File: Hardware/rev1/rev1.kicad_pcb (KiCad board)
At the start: 4 copper layers, 80 x 22 mm, 45 parts, among them J1 Conn_ARM_JTAG_SWD_10, J2 USB_C_Receptacle_USB2.0_14P, J3 Screw_Terminal_01x02, J4 Conn_01x18_Socket, J5 Conn_01x18_Socket, Q1 AO3400A, SW1 SW_Push, U1 W25Q128JVS, U2 HT75xx-1-SOT89, U3 MS5607-02BA, U4 STM32F103C8Tx, Y1 16MHz

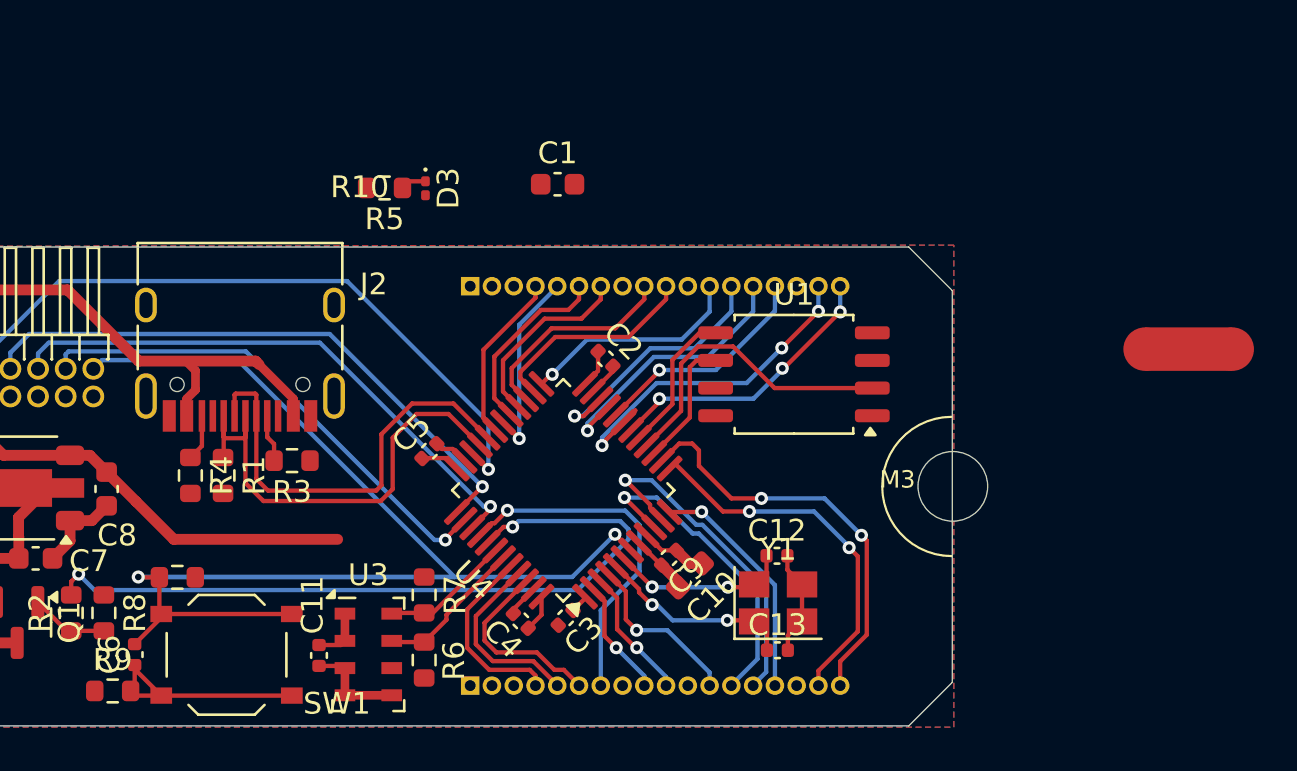
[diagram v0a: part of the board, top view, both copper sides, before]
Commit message: Defenistration Comit
Changed the crystal to be correct, still need to fix the other fixes
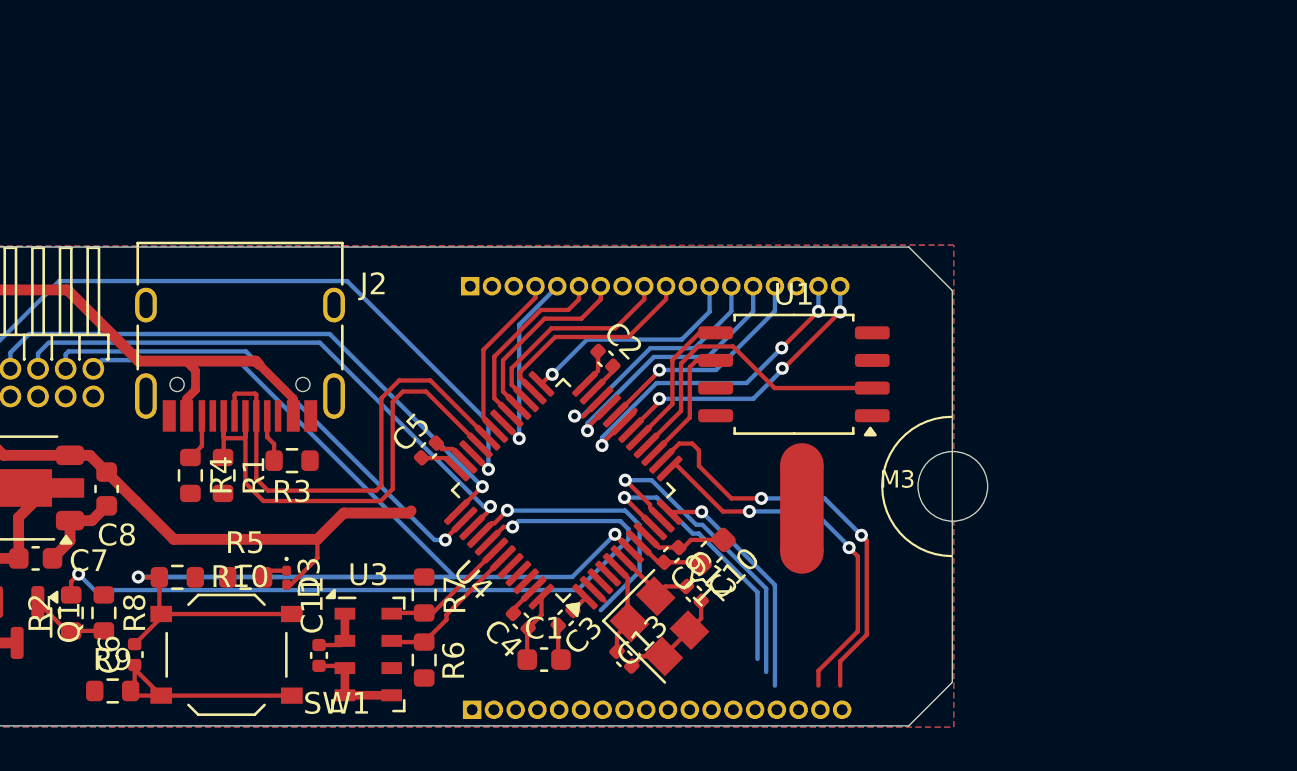
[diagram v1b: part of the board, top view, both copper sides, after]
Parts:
- moved C1 21.8 mm to (174.4, 137.2)
- moved NT1 19.2 mm to (186.2, 130.2), turned to -90 degrees
- moved R5 19.0 mm to (160.7, 133.4)
- moved D3 19.0 mm to (162.6, 133.4)
- moved C13 7.04 mm to (178.1, 137.1), turned to -45 degrees
- moved Y1 5.55 mm to (179.7, 135.6), turned to -45 degrees
- moved C12 4.20 mm to (181.3, 134.1), turned to -45 degrees
- moved C10 1.47 mm to (182.1, 132.2)
- moved J5 1.11 mm to (171.1, 139.5)
- moved C9 0.17 mm to (180.2, 132.3)
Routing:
- net /Microcontroller/PB9: track 8.73 -> 0.00 mm
- net /Microcontroller/BOOTO: track 8.72 -> 0.00 mm
- net /Microcontroller/PB8: track 8.60 -> 0.00 mm
- net +3.3V: track 28.7 -> 36.9 mm
- net /Microcontroller/PC15: track 7.91 -> 0.00 mm, vias 1 -> 0
- net /Microcontroller/PC14: track 6.08 -> 0.00 mm, vias 1 -> 0
- net /Microcontroller/HSE_IN: track 9.53 -> 4.43 mm, vias 2 -> 0
- net /Microcontroller/PC13: track 5.42 -> 0.77 mm, vias 1 -> 0
- net /Microcontroller/HSE_OUT: track 8.52 -> 4.24 mm, vias 2 -> 0
- net /Microcontroller/PB4: track 16.2 -> 12.7 mm
- net GND: track 21.1 -> 23.1 mm
- net /Microcontroller/USB.D-: track 20.4 -> 22.3 mm
- net /Microcontroller/USB.D+: track 22.8 -> 24.6 mm
- net /Microcontroller/PA0: track 14.6 -> 12.9 mm
- net /Microcontroller/PA1: track 15.8 -> 14.9 mm
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
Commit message: No vallium for the whole week :(
Net tie footprint, moved breakouts, crystal we think is close enough, tried to look for debug interface but didn't find it. no vallies :(
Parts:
- removed H3: MountingHole, MountingHole:MountingHole_3.2mm_M3
- NT1: footprint NetTie:NetTie-2_SMD_Pad2.0mm -> NetTie:NetTie-2_SMD_Pad0.5mm
- moved J4 82.2 mm to (120.0, 55.5)
- moved J5 81.3 mm to (120.0, 76.2)
- moved BT1 80.8 mm to (77.8, 65.8)
- moved BZ1 80.8 mm to (94.7, 70.7)
- moved C1 80.8 mm to (124.2, 73.8)
- moved C10 80.8 mm to (131.9, 68.8)
- moved C11 80.8 mm to (113.9, 73.6)
- moved C13 80.8 mm to (127.9, 73.7)
- moved C3 80.8 mm to (125.2, 71.9)
- moved C6 80.8 mm to (105.4, 73.6)
- moved C9 80.8 mm to (130.1, 69.0)
- moved J2 80.8 mm to (110.2, 58.5)
- moved J3 80.8 mm to (91.8, 61.6)
- moved R1 80.8 mm to (109.5, 65.3)
- moved R4 80.8 mm to (108.0, 65.3)
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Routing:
- net /Microcontroller/PA4: track 19.2 -> 0.00 mm, vias 2 -> 0
- net /Microcontroller/PA3: track 17.2 -> 0.34 mm, vias 2 -> 0
- net /Microcontroller/PB1: track 16.9 -> 0.00 mm, vias 3 -> 0
- net /Microcontroller/PA1: track 14.9 -> 0.00 mm, vias 1 -> 0
- net /Microcontroller/PB0: track 13.2 -> 0.00 mm, vias 3 -> 0
- net /Microcontroller/PA0: track 12.9 -> 0.00 mm, vias 1 -> 0
- net /Microcontroller/PB4: track 12.7 -> 0.00 mm, vias 1 -> 0
- net /Microcontroller/PB10: track 12.7 -> 0.00 mm, vias 1 -> 0
- net /Microcontroller/PB11: track 11.9 -> 0.00 mm, vias 1 -> 0
- net /Microcontroller/PA2: track 10.9 -> 0.00 mm, vias 1 -> 0
- net /Microcontroller/PB2: track 10.5 -> 0.00 mm, vias 1 -> 0
- net /Microcontroller/PB12: track 10.3 -> 0.00 mm, vias 1 -> 0
- net /Microcontroller/PB13: track 9.84 -> 0.00 mm
- net /Microcontroller/PB14: track 9.71 -> 0.00 mm
- net /Microcontroller/PA9: track 8.77 -> 0.03 mm, vias 1 -> 0
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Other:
- outline, holes or cut-outs redrawn

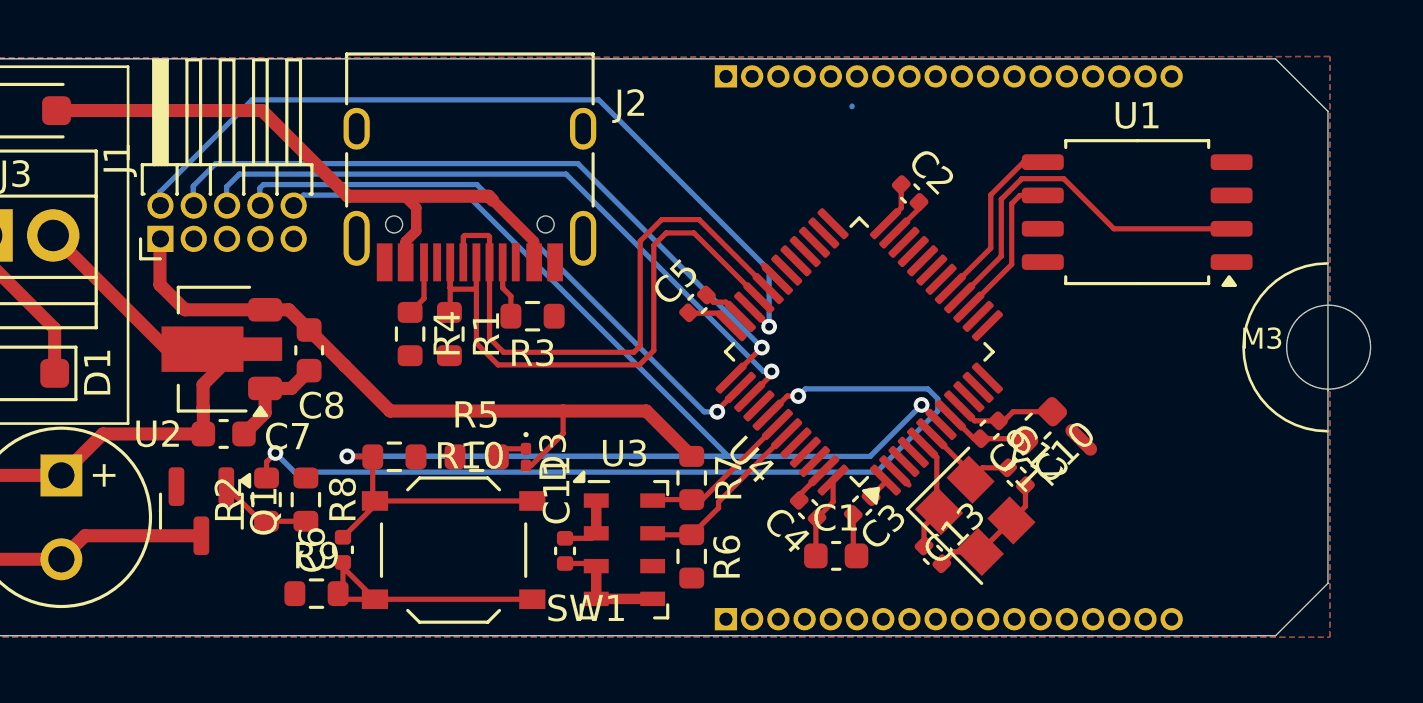
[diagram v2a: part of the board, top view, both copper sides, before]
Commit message: Discarded a bunch of headers, finished traces, need stitching vias
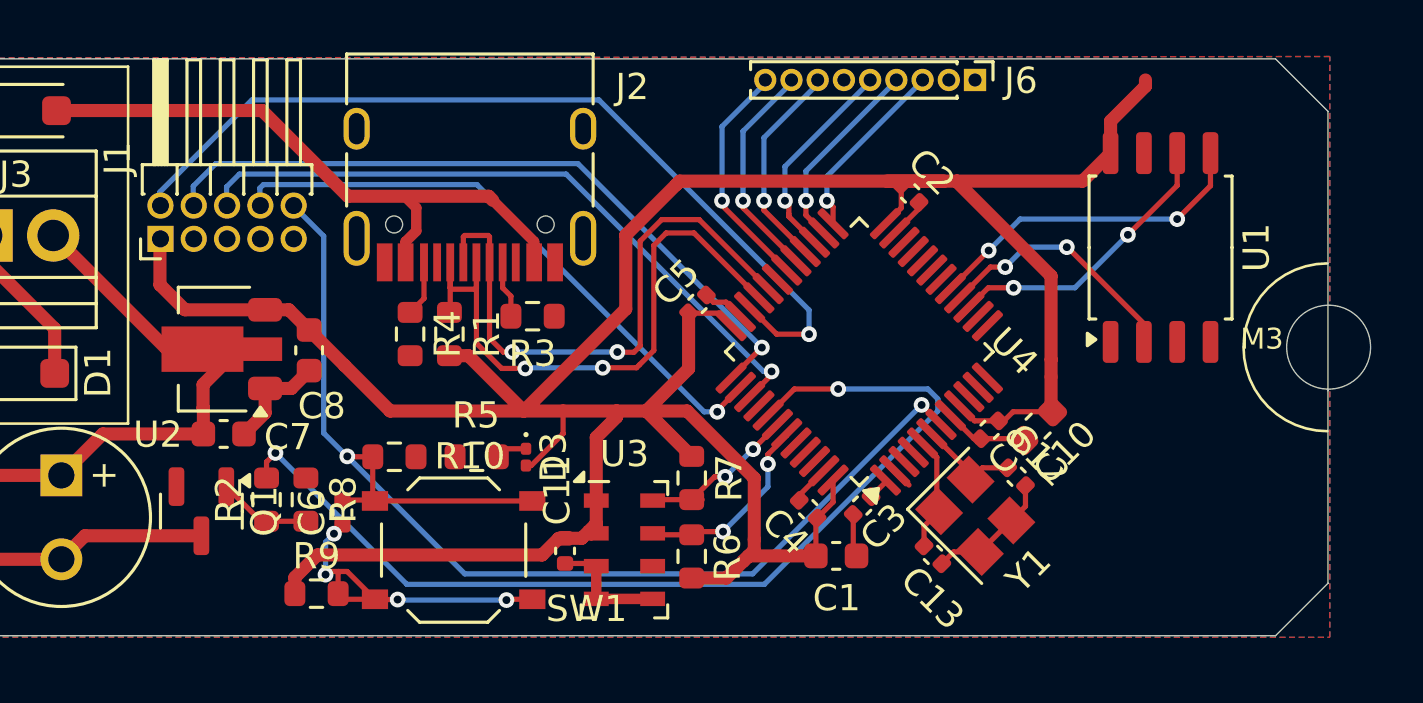
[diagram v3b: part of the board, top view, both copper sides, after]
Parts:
- removed J4, J5: Conn_01x18_Socket, Connector_PinHeader_1.00mm:PinHeader_1x18_P1.00mm_Vertical
- added J6: Conn_01x09_Socket, Connector_PinHeader_1.00mm:PinHeader_1x09_P1.00mm_Vertical, F.Cu at (129.5, 55.6)
- moved NT1 2.23 mm to (132.4, 67.5), turned to -90 degrees
- moved U1 1.62 mm to (136.6, 62.0), turned to 90 degrees
- moved C6 1.42 mm to (105.4, 72.1)
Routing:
- net +3.3V: track 37.7 -> 117.7 mm
- net /Microcontroller/DBG.NRESET: track 69.8 -> 47.8 mm
- net /Microcontroller/PA9: track 0.03 -> 8.95 mm, vias 0 -> 1
- net /Microcontroller/PA8: track 0.00 -> 8.50 mm, vias 0 -> 1
- net /Microcontroller/PB15: track 0.00 -> 8.04 mm, vias 0 -> 1
- net /Microcontroller/PB14: track 0.00 -> 8.03 mm, vias 0 -> 1
- net /Microcontroller/PB13: track 0.00 -> 7.55 mm, vias 0 -> 1
- net /Microcontroller/PB12: track 0.00 -> 7.09 mm, vias 0 -> 1
- net /Microcontroller/SPI1.MOSI: track 6.71 -> 12.8 mm, vias 0 -> 2
- net /Microcontroller/SPI1.SCLK: track 5.94 -> 11.1 mm, vias 0 -> 2
- net /Microcontroller/SPI1.MISO: track 14.3 -> 9.73 mm, vias 0 -> 2
- net /Microcontroller/BUZZER: track 35.1 -> 38.7 mm
- net /Microcontroller/DBG.TMS/SWDIO: track 31.1 -> 33.7 mm
- net Net-(C6-Pad1): track 10.7 -> 12.9 mm, vias 0 -> 4
- net /Microcontroller/PA10: track 0.77 -> 0.00 mm
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
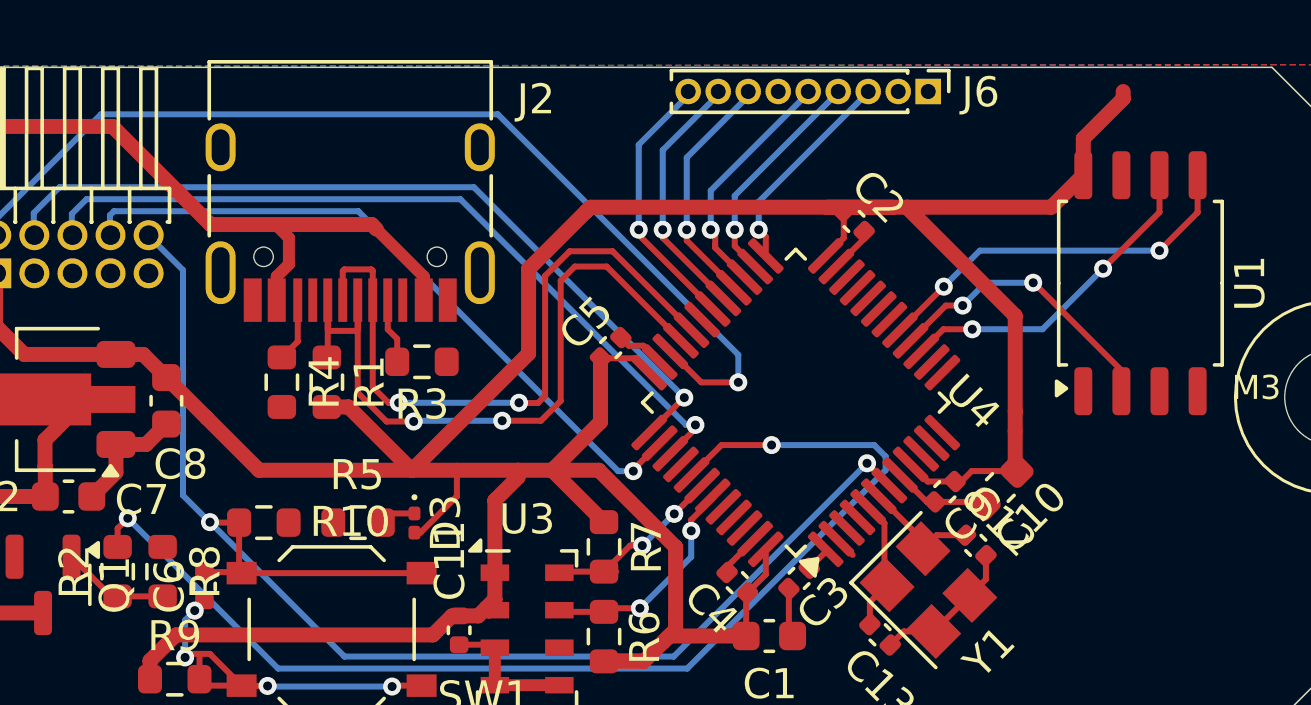
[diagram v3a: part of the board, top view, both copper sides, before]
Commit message: mended power trace on header
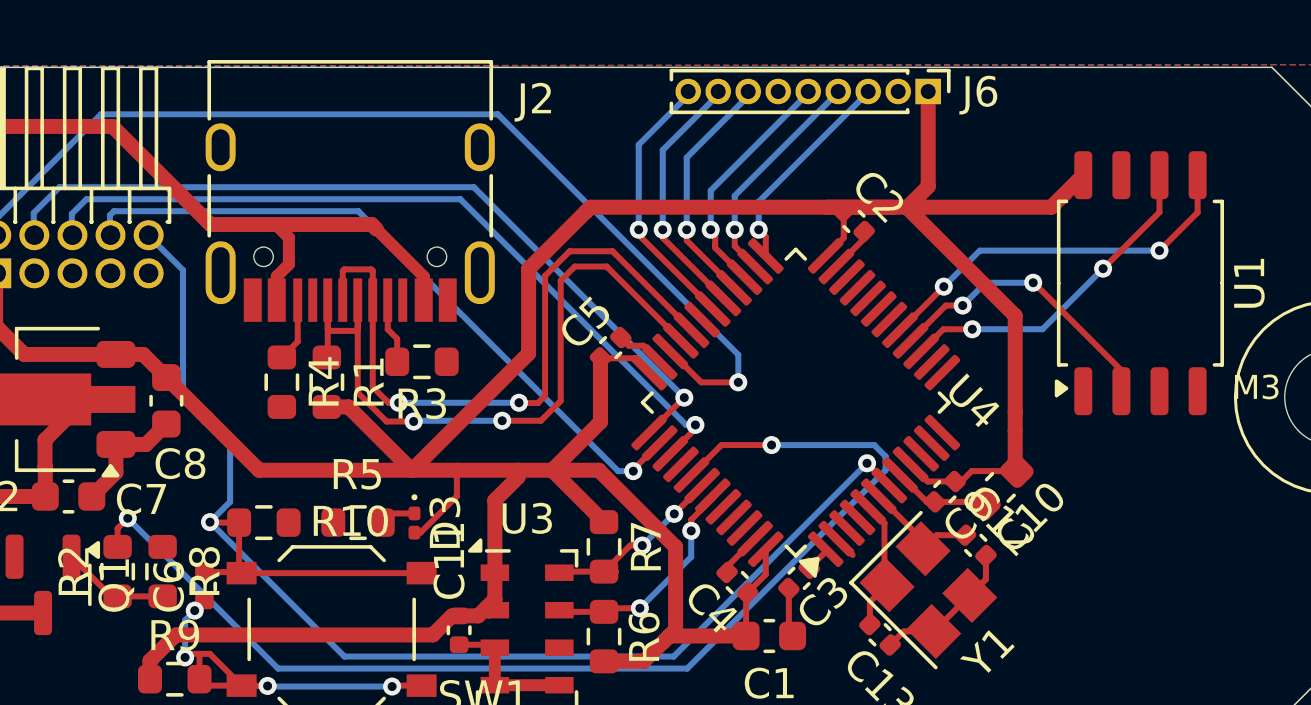
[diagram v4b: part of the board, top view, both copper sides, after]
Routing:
- net +3.3V: track 117.7 -> 118.5 mm
- net /Microcontroller/DBG.NRESET: track 47.8 -> 48.4 mm
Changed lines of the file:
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@@
+	)
+	(segment
+		(start 129.5 58.802464)
+		(end 129.5 55.635)
+		(width 0.5)
+		(layer "F.Cu")
+		(net 5)
 	)
 	(segment
@@
 	)
 	(segment
+		(start 128.81 59.492464)
+		(end 129.5 58.802464)
+		(width 0.5)
+		(layer "F.Cu")
+		(net 5)
+	)
+	(segment
 		(start 121.08 73.57)
 		(end 120.655 73.995)
@@
 	)
 	(segment
-		(start 134.67 57.202437)
-		(end 136 55.872437)
-		(width 0.5)
-		(layer "F.Cu")
-		(net 5)
-	)
-	(segment
 		(start 103.335 64.4)
 		(end 104.105 65.17)
@@
 	)
 	(segment
-		(start 136 55.872437)
-		(end 136 55.635)
-		(width 0.5)
-		(layer "F.Cu")
-		(net 5)
-	)
-	(segment
 		(start 115.055 72.56)
 		(end 114.5 73.115)
@@
 		(start 98.415 63.445)
 		(end 98.415 61.695)
-		(width 0.5)
-		(layer "F.Cu")
-		(net 5)
-	)
-	(segment
-		(start 134.67 58.425)
-		(end 134.67 57.202437)
 		(width 0.5)
 		(layer "F.Cu")
@@
 	)
 	(segment
+		(start 104.66 61.59)
+		(end 103.495 60.425)
+		(width 0.2)
+		(layer "B.Cu")
+		(net 7)
+	)
+	(segment
 		(start 105.56 69.99)
 		(end 110.04 74.47)
@@
 	)
 	(segment
-		(start 104.66 69.1)
-		(end 104.66 61.59)
-		(width 0.2)
-		(layer "B.Cu")
-		(net 7)
-	)
-	(segment
 		(start 121.01912 74.47)
 		(end 127.461337 68.027783)
@@
 	)
 	(segment
+		(start 106.23 67.32)
+		(end 104.66 65.75)
+		(width 0.2)
+		(layer "B.Cu")
+		(net 7)
+	)
+	(segment
+		(start 106.23 69.31)
+		(end 106.23 67.32)
+		(width 0.2)
+		(layer "B.Cu")
+		(net 7)
+	)
+	(segment
 		(start 105.55 69.99)
-		(end 104.66 69.1)
+		(end 106.23 69.31)
 		(width 0.2)
 		(layer "B.Cu")
@@
 	)
 	(segment
-		(start 104.66 61.59)
-		(end 103.495 60.425)
-		(width 0.2)
-		(layer "B.Cu")
+		(start 104.66 65.75)
+		(end 104.66 61.59)
+		(width 0.2)
+		(layer "B.Cu")
